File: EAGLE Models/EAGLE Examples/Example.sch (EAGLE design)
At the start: 2 parts

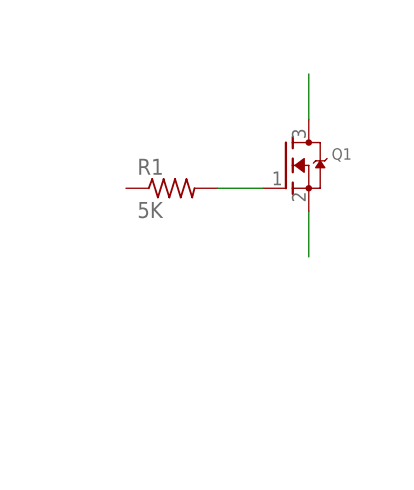
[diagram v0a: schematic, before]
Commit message: Finished Example board for EAGLE tutorial
Did board layout
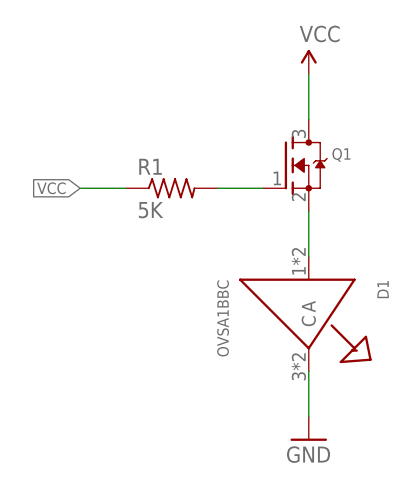
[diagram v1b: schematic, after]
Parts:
- added D1: OVSA1BBC, TTelectronics:OVSA1BBC
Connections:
- net N$1 renamed GATE
- removed net N$2: Q1.D
- removed net N$3: Q1.S
- new net DRIN: D1.A, Q1.S
- new net GND: D1.C
- new net VCC: Q1.D, R1.1
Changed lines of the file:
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@@
 <part name="R1" library="adafruit" deviceset="R-US_" device="M0805" value="5K"/>
 <part name="Q1" library="adafruit" deviceset="MOSFET-N" device="REFLOW"/>
+<part name="D1" library="TTelectronics" deviceset="OVSA1BBC" device=""/>
+<part name="GND1" library="SparkFun-Aesthetics" deviceset="GND" device=""/>
+<part name="SUPPLY1" library="SparkFun-Aesthetics" deviceset="VCC" device=""/>
 </parts>
 <sheets>
@@
 <instance part="R1" gate="G$1" x="5.08" y="7.62"/>
 <instance part="Q1" gate="G$1" x="17.78" y="10.16"/>
+<instance part="D1" gate="G$1" x="20.32" y="-5.08" rot="R270"/>
+<instance part="GND1" gate="1" x="20.32" y="-20.32"/>
+<instance part="SUPPLY1" gate="1" x="20.32" y="20.32"/>
 </instances>
 <busses>
 </busses>
 <nets>
-<net name="N$1" class="0">
+<net name="GATE" class="0">
 <segment>
 <pinref part="R1" gate="G$1" pin="2"/>
@@
 </segment>
 </net>
-<net name="N$2" class="0">
+<net name="DRIN" class="0">
+<segment>
+<pinref part="Q1" gate="G$1" pin="S"/>
+<wire x1="20.32" y1="5.08" x2="20.32" y2="0" width="0.1524" layer="91"/>
+<pinref part="D1" gate="G$1" pin="A"/>
+</segment>
+</net>
+<net name="GND" class="0">
+<segment>
+<pinref part="D1" gate="G$1" pin="C"/>
+<wire x1="20.32" y1="-12.7" x2="20.32" y2="-17.78" width="0.1524" layer="91"/>
+<pinref part="GND1" gate="1" pin="GND"/>
+</segment>
+</net>
+<net name="VCC" class="0">
+<segment>
+<pinref part="R1" gate="G$1" pin="1"/>
+<wire x1="0" y1="7.62" x2="-5.08" y2="7.62" width="0.1524" layer="91"/>
+<label x="-5.08" y="7.62" size="1.27" layer="95" rot="R180" xref="yes"/>
+</segment>
 <segment>
 <pinref part="Q1" gate="G$1" pin="D"/>
 <wire x1="20.32" y1="15.24" x2="20.32" y2="20.32" width="0.1524" layer="91"/>
+<pinref part="SUPPLY1" gate="1" pin="VCC"/>
 </segment>
 </net>
-<net name="N$3" class="0">
-<segment>
-<pinref part="Q1" gate="G$1" pin="S"/>
-<wire x1="20.32" y1="5.08" x2="20.32" y2="0" width="0.1524" layer="91"/>
-</segment>
-</net>
